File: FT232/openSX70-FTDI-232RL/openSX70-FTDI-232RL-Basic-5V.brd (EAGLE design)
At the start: 27.9 x 17.3 mm, 16 parts, among them J1 687106183722, U1 FT232RLSSOP

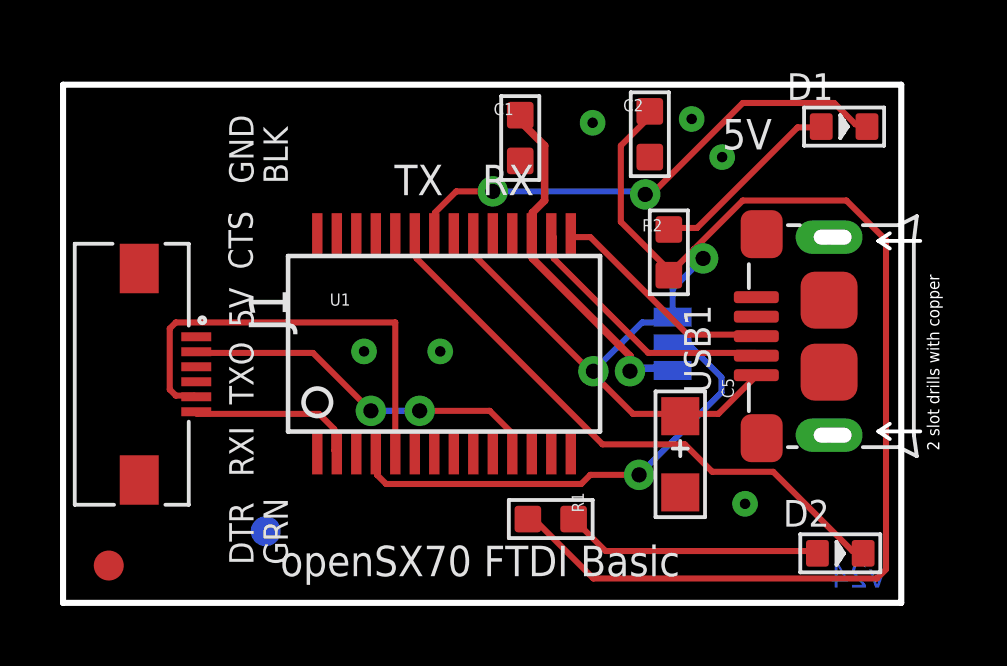
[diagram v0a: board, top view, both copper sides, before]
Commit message: NEW FTDI for manufacture 232RL based on Sparkfun FTDI basic
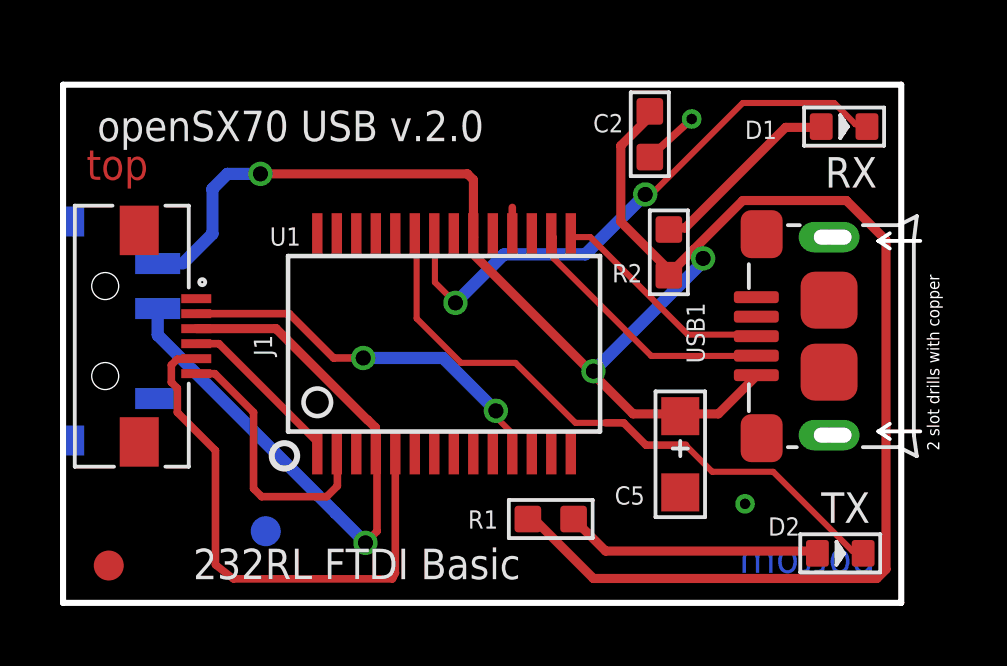
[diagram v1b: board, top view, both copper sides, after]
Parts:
- removed C1: 100nf, openSX70_PATHFINDER_V5.5-SEEED_20180522:C0603
- removed JP2: LOGO-SFESK, SparkFun:SFE-LOGO-FLAME
- removed LOGO1: OSHW-LOGOS, SparkFun-Aesthetics:OSHW-LOGO-S
- removed SJ2: (no value), SparkFun:SJ_3
- added S1: (no value), SparkFun-Switches:SWITCH_SPST_SMD_A
- moved J1 1.27 mm to (-2.54, 8.89)
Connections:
- removed net 3.3V: C1.1, SJ2.3, U1.17
- net 5V: now also S1.1; no longer SJ2.1
- net GND: no longer C1.2
- net POWER: now also S1.2; no longer SJ2.2
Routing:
- net 5V: track 58.5 -> 72.6 mm, vias 2 -> 3
- net 3.3V: track 11.9 -> 0.00 mm, vias 1 -> 0
- net POWER: track 16.2 -> 22.1 mm
- net TXO: track 0.00 -> 5.77 mm
- net RXI: track 15.0 -> 18.5 mm
- net DTR: track 5.70 -> 9.13 mm
- net GND: track 0.00 -> 2.78 mm, vias 6 -> 2
- net RXLED: track 17.1 -> 19.4 mm
- net TXLED: track 19.8 -> 21.0 mm
- net CTS: track 12.3 -> 13.0 mm
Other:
- board text added: "232RL FTDI Basic"
- board text added: "bottom"
- board text added: "openSX70 USB v.2.0"
- board text added: "top"
- board text removed: "3.3V"
- board text removed: "5V"
- board text removed: "BLK"
- board text removed: "CTS"
- board text removed: "Close"
- board text removed: "DTR"
- board text removed: "GND"
- board text removed: "GRN"
- board text removed: "RXI"
- board text removed: "TXO"
- board text removed: "openSX70 FTDI Basic"
- board text removed: "v24"

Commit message: Fixes to power.
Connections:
- new net N$4: U1.20, U1.4
- net 5V: no longer U1.20
- net POWER: no longer U1.4
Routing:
- net POWER: track 22.1 -> 21.2 mm
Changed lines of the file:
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@@
 <?xml version="1.0" encoding="utf-8"?>
 <!DOCTYPE eagle SYSTEM "eagle.dtd">
-<eagle version="9.1.0">
+<eagle version="9.0.0">
 <drawing>
 <settings>
@@
 <param name="checkStop" value="0"/>
 <param name="checkValues" value="0"/>
-<param name="checkNames" value="1"/>
-<param name="checkWireStubs" value="1"/>
-<param name="checkPolygonWidth" value="0"/>
 <param name="useDiameter" value="13"/>
 <param name="maxErrors" value="50"/>
@@
 </signal>
 <signal name="POWER">
-<contactref element="U1" pad="4"/>
 <contactref element="J1" pad="3"/>
 <wire x1="5.3848" y1="4.9784" x2="5.3848" y2="4.2672" width="0.2032" layer="1"/>
-<wire x1="5.3848" y1="4.9784" x2="5.345" y2="4.98" width="0.2032" layer="1"/>
 <wire x1="-0.64" y1="9.14" x2="2.02" y2="9.14" width="0.3048" layer="1"/>
 <wire x1="5.064" y1="6.096" x2="2.02" y2="9.14" width="0.3048" layer="1"/>
-<wire x1="5.345" y1="4.98" x2="5.334" y2="5.842" width="0.3048" layer="1"/>
 <wire x1="5.334" y1="5.842" x2="5.08" y2="6.096" width="0.3048" layer="1"/>
 <wire x1="5.08" y1="6.096" x2="5.064" y2="6.096" width="0.254" layer="1"/>
@@
 <wire x1="5.3848" y1="2.3848" x2="5.3848" y2="4.2672" width="0.254" layer="1"/>
 <wire x1="-1.925" y1="8.925" x2="4" y2="3" width="0.4064" layer="16"/>
+<wire x1="5.3848" y1="4.9784" x2="5.334" y2="5.842" width="0" layer="19" extent="1-1"/>
 </signal>
 <signal name="5V">
-<contactref element="U1" pad="20"/>
 <contactref element="C5" pad="+"/>
 <contactref element="C2" pad="1"/>
@@
 <wire x1="12.5476" y1="7.6708" x2="8.636" y2="11.5824" width="0.3048" layer="1"/>
 <wire x1="15.4432" y1="6.2992" x2="13.9192" y2="6.2992" width="0.3048" layer="1"/>
-<wire x1="8.636" y1="12.192" x2="8.595" y2="12.292" width="0.2032" layer="1"/>
 <wire x1="15.4432" y1="6.2992" x2="15.494" y2="6.223" width="0.2032" layer="1"/>
 <wire x1="10.668" y1="2.7432" x2="10.4648" y2="2.7432" width="0.2032" layer="1"/>
@@
 <wire x1="18.03" y1="8.24" x2="18.0212" y2="8.2312" width="0.2032" layer="1"/>
 </signal>
+<signal name="N$4">
+<contactref element="U1" pad="4"/>
+<contactref element="U1" pad="20"/>
+<wire x1="5.345" y1="4.98" x2="8.595" y2="12.292" width="0" layer="19" extent="1-1"/>
+</signal>
 </signals>
-<mfgpreviewcolors>
-<mfgpreviewcolor name="soldermaskcolor" color="0xC8008000"/>
-<mfgpreviewcolor name="silkscreencolor" color="0xFFFEFEFE"/>
-<mfgpreviewcolor name="backgroundcolor" color="0xFF282828"/>
-<mfgpreviewcolor name="coppercolor" color="0xFFFFBF00"/>
-<mfgpreviewcolor name="substratecolor" color="0xFF786E46"/>
-</mfgpreviewcolors>
 <errors>
 </errors>

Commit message: Upgrade to 9.1.1 and fixes
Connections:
- net POWER renamed N$5
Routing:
- net N$5: track 21.2 -> 0.00 mm, vias 1 -> 0
- net GND: track 2.78 -> 1.11 mm, vias 2 -> 1
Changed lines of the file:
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@@
 <?xml version="1.0" encoding="utf-8"?>
 <!DOCTYPE eagle SYSTEM "eagle.dtd">
-<eagle version="9.0.0">
+<eagle version="9.1.1">
 <drawing>
 <settings>
@@
 <layer number="14" name="Route14" color="1" fill="6" visible="no" active="no"/>
 <layer number="15" name="Route15" color="4" fill="6" visible="no" active="no"/>
-<layer number="16" name="Bottom" color="1" fill="1" visible="no" active="yes"/>
+<layer number="16" name="Bottom" color="1" fill="1" visible="yes" active="yes"/>
 <layer number="17" name="Pads" color="2" fill="1" visible="yes" active="yes"/>
 <layer number="18" name="Vias" color="2" fill="1" visible="yes" active="yes"/>
@@
 <param name="checkStop" value="0"/>
 <param name="checkValues" value="0"/>
+<param name="checkNames" value="1"/>
+<param name="checkWireStubs" value="1"/>
+<param name="checkPolygonWidth" value="0"/>
 <param name="useDiameter" value="13"/>
 <param name="maxErrors" value="50"/>
@@
 <param name="RoutingGrid" value="50mil"/>
 <param name="AutoGrid" value="1"/>
-<param name="Efforts" value="0"/>
+<param name="Efforts" value="2"/>
 <param name="TopRouterVariant" value="1"/>
 <param name="tpViaShape" value="round"/>
-<param name="PrefDir.1" value="|"/>
+<param name="PrefDir.1" value="a"/>
 <param name="PrefDir.2" value="0"/>
 <param name="PrefDir.3" value="0"/>
@@
 <param name="PrefDir.14" value="0"/>
 <param name="PrefDir.15" value="0"/>
-<param name="PrefDir.16" value="-"/>
+<param name="PrefDir.16" value="a"/>
 <param name="cfVia" value="8"/>
 <param name="cfNonPref" value="5"/>
@@
 <contactref element="USB1" pad="5"/>
 <contactref element="J1" pad="1"/>
-<via x="17.653" y="3.302" extent="1-16" drill="0.35"/>
-<via x="15.875" y="16.129" extent="1-16" drill="0.35"/>
-<wire x1="9.895" y1="12.292" x2="9.895" y2="13.18" width="0.254" layer="1"/>
-<wire x1="14.478" y1="14.859" x2="15.875" y2="16.129" width="0.254" layer="1"/>
+<wire x1="15.0241" y1="14.9352" x2="14.4907" y2="14.9352" width="0.254" layer="1"/>
+<wire x1="15.3797" y1="15.2908" x2="15.0241" y2="14.9352" width="0.254" layer="1"/>
+<wire x1="14.4907" y1="14.9352" x2="14.478" y2="14.859" width="0.254" layer="1"/>
+<via x="15.3797" y="15.2908" extent="1-16" drill="0.3048"/>
+<wire x1="15.494" y1="3.683" x2="18.207" y2="5.49" width="0" layer="19" extent="1-1"/>
 </signal>
 <signal name="USB_D+">
@@
 <wire x1="5.995" y1="1.005" x2="5.995" y2="4.98" width="0.254" layer="1"/>
 </signal>
-<signal name="POWER">
-<contactref element="J1" pad="3"/>
-<wire x1="5.3848" y1="4.9784" x2="5.3848" y2="4.2672" width="0.2032" layer="1"/>
-<wire x1="-0.64" y1="9.14" x2="2.02" y2="9.14" width="0.3048" layer="1"/>
-<wire x1="5.064" y1="6.096" x2="2.02" y2="9.14" width="0.3048" layer="1"/>
-<wire x1="5.334" y1="5.842" x2="5.08" y2="6.096" width="0.3048" layer="1"/>
-<wire x1="5.08" y1="6.096" x2="5.064" y2="6.096" width="0.254" layer="1"/>
-<contactref element="S1" pad="2"/>
-<wire x1="-1.925" y1="9.81" x2="-1.925" y2="8.925" width="0.4064" layer="16"/>
-<wire x1="4" y1="3" x2="5" y2="2" width="0.4064" layer="16"/>
-<via x="5" y="2" extent="1-16" drill="0.508"/>
-<wire x1="5" y1="2" x2="5.3848" y2="2.3848" width="0.254" layer="1"/>
-<wire x1="5.3848" y1="2.3848" x2="5.3848" y2="4.2672" width="0.254" layer="1"/>
-<wire x1="-1.925" y1="8.925" x2="4" y2="3" width="0.4064" layer="16"/>
-<wire x1="5.3848" y1="4.9784" x2="5.334" y2="5.842" width="0" layer="19" extent="1-1"/>
-</signal>
 <signal name="5V">
 <contactref element="C5" pad="+"/>
@@
 <wire x1="15.5448" y1="6.2992" x2="15.494" y2="6.223" width="0.2032" layer="1"/>
 <wire x1="17.9832" y1="7.5184" x2="18.03" y2="7.59" width="0.2032" layer="1"/>
-<wire x1="8.636" y1="11.5824" x2="8.636" y2="11.9" width="0.2032" layer="1"/>
-<wire x1="8.636" y1="11.9" x2="8.636" y2="12.192" width="0.2032" layer="1"/>
+<wire x1="8.636" y1="11.5824" x2="8.636" y2="12.192" width="0.2032" layer="1"/>
 <wire x1="13.9192" y1="6.2992" x2="12.5476" y2="7.6708" width="0.3048" layer="1"/>
 <wire x1="12.5476" y1="7.6708" x2="8.636" y2="11.5824" width="0.3048" layer="1"/>
@@
 <wire x1="5.345" y1="4.98" x2="8.595" y2="12.292" width="0" layer="19" extent="1-1"/>
 </signal>
+<signal name="N$5">
+<contactref element="S1" pad="2"/>
+<contactref element="J1" pad="3"/>
+<wire x1="-0.64" y1="9.14" x2="-1.925" y2="9.81" width="0" layer="19" extent="1-16"/>
+</signal>
 </signals>
+<mfgpreviewcolors>
+<mfgpreviewcolor name="soldermaskcolor" color="0xC8008000"/>
+<mfgpreviewcolor name="silkscreencolor" color="0xFFFEFEFE"/>
+<mfgpreviewcolor name="backgroundcolor" color="0xFF282828"/>
+<mfgpreviewcolor name="coppercolor" color="0xFFFFBF00"/>
+<mfgpreviewcolor name="substratecolor" color="0xFF786E46"/>
+</mfgpreviewcolors>
 <errors>
 </errors>

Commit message: new FTDI FT232RL for manufacturing
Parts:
- renumbered C5 to C1
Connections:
- net N$5 renamed 5V-J1
- removed net N$4: U1.20, U1.4
- net 5V: now also U1.20, U1.4
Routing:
- net 5V: track 72.5 -> 86.3 mm
- net 5V-J1: track 0.00 -> 8.14 mm, vias 0 -> 1
- net GND: track 1.11 -> 2.52 mm, vias 1 -> 4
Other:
- board text added: "openSX70 USB v.2.1"
- board text removed: "openSX70 USB v.2.0"
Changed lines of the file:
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@@
 <?xml version="1.0" encoding="utf-8"?>
 <!DOCTYPE eagle SYSTEM "eagle.dtd">
-<eagle version="9.1.1">
+<eagle version="9.1.0">
 <drawing>
 <settings>
@@
 <text x="22" y="1" size="1.016" layer="16" font="vector" ratio="16" rot="MR0">bottom</text>
 <text x="-4.3" y="14.1" size="1.016" layer="1" font="vector" ratio="16">top</text>
-<text x="-3.941" y="15.389" size="1.016" layer="21" font="vector" ratio="15">openSX70 USB v.2.0</text>
+<text x="-3.941" y="15.389" size="1.016" layer="21" font="vector" ratio="15">openSX70 USB v.2.1</text>
 <circle x="2.3" y="4.9" radius="0.4242625" width="0.2" layer="21"/>
 </plain>
@@
 <attribute name="VALUE" value="100nf" x="15.748" y="15.494" size="0.4064" layer="27" font="vector"/>
 </element>
-<element name="C5" library="Seeed-Capacitor-2016" package="AVX-A" value="10uf" x="15.494" y="4.953" smashed="yes" rot="R270">
+<element name="C1" library="Seeed-Capacitor-2016" package="AVX-A" value="10uf" x="15.494" y="4.953" smashed="yes" rot="R270">
 <attribute name="MPN" value="TAJA106K016RNJ" x="15.494" y="4.953" size="1.778" layer="27" rot="R270" display="off"/>
 <attribute name="NAME" x="13.307" y="3.275" size="0.6096" layer="25" font="vector" ratio="16"/>
@@
 <signal name="GND" class="1">
 <contactref element="C2" pad="2"/>
-<contactref element="C5" pad="-"/>
+<contactref element="C1" pad="-"/>
 <contactref element="U1" pad="26"/>
 <contactref element="U1" pad="25"/>
@@
 <contactref element="USB1" pad="5"/>
 <contactref element="J1" pad="1"/>
-<wire x1="15.0241" y1="14.9352" x2="14.4907" y2="14.9352" width="0.254" layer="1"/>
-<wire x1="15.3797" y1="15.2908" x2="15.0241" y2="14.9352" width="0.254" layer="1"/>
+<wire x1="14.4907" y1="14.9352" x2="14.5241" y2="14.9352" width="0.254" layer="1"/>
 <wire x1="14.4907" y1="14.9352" x2="14.478" y2="14.859" width="0.254" layer="1"/>
-<via x="15.3797" y="15.2908" extent="1-16" drill="0.3048"/>
-<wire x1="15.494" y1="3.683" x2="18.207" y2="5.49" width="0" layer="19" extent="1-1"/>
+<via x="15.8797" y="16.2908" extent="1-16" drill="0.3048"/>
+<via x="18" y="3" extent="1-16" drill="0.35"/>
+<via x="10.9" y="14.4" extent="1-16" drill="0.35"/>
+<wire x1="14.5241" y1="14.9352" x2="14.5241" y2="14.9352" width="0.254" layer="1"/>
+<wire x1="15.8797" y1="16.2908" x2="16" y2="16.1705" width="0.3048" layer="1"/>
+<wire x1="16" y1="16" x2="16" y2="16.1705" width="0.3048" layer="1"/>
+<wire x1="14.478" y1="14.859" x2="14.6885" y2="14.859" width="0.3048" layer="1"/>
+<wire x1="14.6885" y1="14.859" x2="16" y2="16.1705" width="0.3048" layer="1"/>
+<via x="5.5" y="10.7" extent="1-16" drill="0.35"/>
 </signal>
 <signal name="USB_D+">
@@
 <contactref element="U1" pad="11"/>
 <contactref element="J1" pad="2"/>
-<wire x1="7.5852" y1="8.1628" x2="4.9276" y2="8.1628" width="0.4064" layer="16"/>
+<wire x1="7.5852" y1="8.1628" x2="4.9276" y2="8.1628" width="0.254" layer="16"/>
 <wire x1="9.3472" y1="6.4008" x2="9.3472" y2="6.1976" width="0.2032" layer="1"/>
 <wire x1="9.8552" y1="5.6896" x2="9.3472" y2="6.1976" width="0.2032" layer="1"/>
@@
 <via x="4.9276" y="8.1628" extent="1-16" drill="0.508"/>
 <via x="9.3472" y="6.4008" extent="1-16" drill="0.508"/>
-<wire x1="9.3472" y1="6.4008" x2="7.5852" y2="8.1628" width="0.4064" layer="16"/>
+<wire x1="9.3472" y1="6.4008" x2="7.5852" y2="8.1628" width="0.254" layer="16"/>
 <wire x1="-0.64" y1="9.64" x2="2.46" y2="9.64" width="0.254" layer="1"/>
 <wire x1="3.9372" y1="8.1628" x2="4.9276" y2="8.1628" width="0.254" layer="1"/>
@@
 <wire x1="21.336" y1="15.9512" x2="21.6408" y2="15.9512" width="0.2032" layer="1"/>
 <wire x1="20.6248" y1="16.6624" x2="21.336" y2="15.9512" width="0.2032" layer="1"/>
-<wire x1="17.5768" y1="16.6624" x2="20.6248" y2="16.6624" width="0.2032" layer="1"/>
-<wire x1="14.5288" y1="13.6144" x2="17.5768" y2="16.6624" width="0.2032" layer="1"/>
-<wire x1="14.3256" y1="13.6144" x2="14.5288" y2="13.6144" width="0.2032" layer="1"/>
+<wire x1="18.5768" y1="16.6624" x2="20.6248" y2="16.6624" width="0.2032" layer="1"/>
+<wire x1="15.5288" y1="13.6144" x2="18.5768" y2="16.6624" width="0.2032" layer="1"/>
+<wire x1="14.3256" y1="13.6144" x2="15.5288" y2="13.6144" width="0.2032" layer="1"/>
 <wire x1="21.6408" y1="15.9512" x2="21.717" y2="15.875" width="0.2032" layer="1"/>
 <wire x1="7.3152" y1="12.2936" x2="7.295" y2="12.292" width="0.2032" layer="1"/>
 <via x="14.3256" y="13.6144" extent="1-16" drill="0.508"/>
-<wire x1="8" y1="10" x2="9.6152" y2="11.6152" width="0.4064" layer="16"/>
+<wire x1="8" y1="10" x2="9.6152" y2="11.6152" width="0.254" layer="16"/>
 <via x="8" y="10" extent="1-16" drill="0.508"/>
 <wire x1="7.3152" y1="10.6848" x2="7.3152" y2="12.2936" width="0.2032" layer="1"/>
 <wire x1="8" y1="10" x2="7.3152" y2="10.6848" width="0.2032" layer="1"/>
-<wire x1="9.6152" y1="11.6152" x2="12.3264" y2="11.6152" width="0.4064" layer="16"/>
-<wire x1="12.3264" y1="11.6152" x2="14.3256" y2="13.6144" width="0.4064" layer="16"/>
+<wire x1="9.6152" y1="11.6152" x2="12.3264" y2="11.6152" width="0.254" layer="16"/>
+<wire x1="12.3264" y1="11.6152" x2="14.3256" y2="13.6144" width="0.254" layer="16"/>
 </signal>
 <signal name="N$1">
@@
 </signal>
 <signal name="5V">
-<contactref element="C5" pad="+"/>
+<contactref element="C1" pad="+"/>
 <contactref element="C2" pad="1"/>
 <contactref element="R1" pad="2"/>
@@
 <wire x1="10.4648" y1="2.7432" x2="10.414" y2="2.794" width="0.2032" layer="1"/>
 <wire x1="15.1384" y1="10.9728" x2="15.113" y2="10.922" width="0.2032" layer="1"/>
-<wire x1="14.4272" y1="16.1544" x2="14.4272" y2="16.3576" width="0.2032" layer="1"/>
-<wire x1="13.5128" y1="15.24" x2="14.4272" y2="16.1544" width="0.3048" layer="1"/>
-<wire x1="13.5128" y1="12.7" x2="13.5128" y2="15.24" width="0.3048" layer="1"/>
-<wire x1="15.1384" y1="11.0744" x2="13.5128" y2="12.7" width="0.3048" layer="1"/>
-<wire x1="14.4272" y1="16.3576" x2="14.478" y2="16.383" width="0.2032" layer="1"/>
+<wire x1="12.5128" y1="15.24" x2="13.6558" y2="16.383" width="0.3048" layer="1"/>
+<wire x1="12.5128" y1="13.7" x2="12.5128" y2="15.24" width="0.3048" layer="1"/>
+<wire x1="15.1384" y1="11.0744" x2="12.5128" y2="13.7" width="0.3048" layer="1"/>
 <wire x1="15.1384" y1="11.0744" x2="15.113" y2="10.922" width="0.2032" layer="1"/>
-<wire x1="15.9512" y1="11.7856" x2="16.256" y2="11.4808" width="0.2032" layer="1"/>
+<wire x1="15.9512" y1="11.7856" x2="16.256" y2="11.4808" width="0.3048" layer="1"/>
 <wire x1="12.5984" y1="7.7216" x2="12.5476" y2="7.6708" width="0.2032" layer="1"/>
 <via x="16.256" y="11.4808" extent="1-16" drill="0.508"/>
@@
 <wire x1="12.5984" y1="7.7216" x2="16.256" y2="11.3792" width="0.4064" layer="16"/>
 <wire x1="16.256" y1="11.3792" x2="16.256" y2="11.4808" width="0.3048" layer="16"/>
+<contactref element="U1" pad="4"/>
+<contactref element="U1" pad="20"/>
+<wire x1="5.345" y1="4.98" x2="5.345" y2="7.345" width="0.3048" layer="1"/>
+<wire x1="5.345" y1="7.345" x2="6" y2="8" width="0.3048" layer="1"/>
+<wire x1="6" y1="8" x2="6" y2="8.7" width="0.3048" layer="1"/>
+<wire x1="6" y1="8.7" x2="3.9" y2="10.8" width="0.3048" layer="1"/>
+<wire x1="1.5" y1="14.3" x2="1.5" y2="11.8" width="0.3048" layer="1"/>
+<wire x1="3.9" y1="10.8" x2="2.3" y2="10.8" width="0.3048" layer="1"/>
+<wire x1="2.3" y1="10.8" x2="1.5" y2="11.8" width="0.3048" layer="1"/>
+<wire x1="13.6558" y1="16.383" x2="14.478" y2="16.383" width="0.3048" layer="1"/>
+<wire x1="8.595" y1="12.292" x2="8.636" y2="12.292" width="0.254" layer="1"/>
+<wire x1="8.636" y1="12.292" x2="8.636" y2="12.192" width="0.254" layer="1"/>
 </signal>
 <signal name="N$3">
@@
 <wire x1="18.03" y1="8.24" x2="18.0212" y2="8.2312" width="0.2032" layer="1"/>
 </signal>
-<signal name="N$4">
-<contactref element="U1" pad="4"/>
-<contactref element="U1" pad="20"/>
-<wire x1="5.345" y1="4.98" x2="8.595" y2="12.292" width="0" layer="19" extent="1-1"/>
-</signal>
-<signal name="N$5">
+<signal name="5V-J1">
 <contactref element="S1" pad="2"/>
 <contactref element="J1" pad="3"/>
-<wire x1="-0.64" y1="9.14" x2="-1.925" y2="9.81" width="0" layer="19" extent="1-16"/>
+<wire x1="1.446665625" y1="9.14" x2="1.46" y2="9.14" width="0.3048" layer="1"/>
+<wire x1="1.498078125" y1="9.101921875" x2="2.3" y2="8.3" width="0.3048" layer="1"/>
+<via x="2.3" y="8.3" extent="1-16" drill="0.35"/>
+<wire x1="2.3" y1="8.3" x2="0.79" y2="9.81" width="0.3048" layer="16"/>
+<wire x1="0.79" y1="9.81" x2="-1.925" y2="9.81" width="0.3048" layer="16"/>
+<wire x1="-0.64" y1="9.14" x2="1.446665625" y2="9.14" width="0.3048" layer="1"/>
+<wire x1="1.46" y1="9.14" x2="1.498078125" y2="9.101921875" width="0.3048" layer="1"/>
 </signal>
 </signals>
